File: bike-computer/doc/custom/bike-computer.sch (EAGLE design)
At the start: 12 parts, among them Q1 2N3820, Q2 2N3820, Q3 2N3820, X1 5566-8

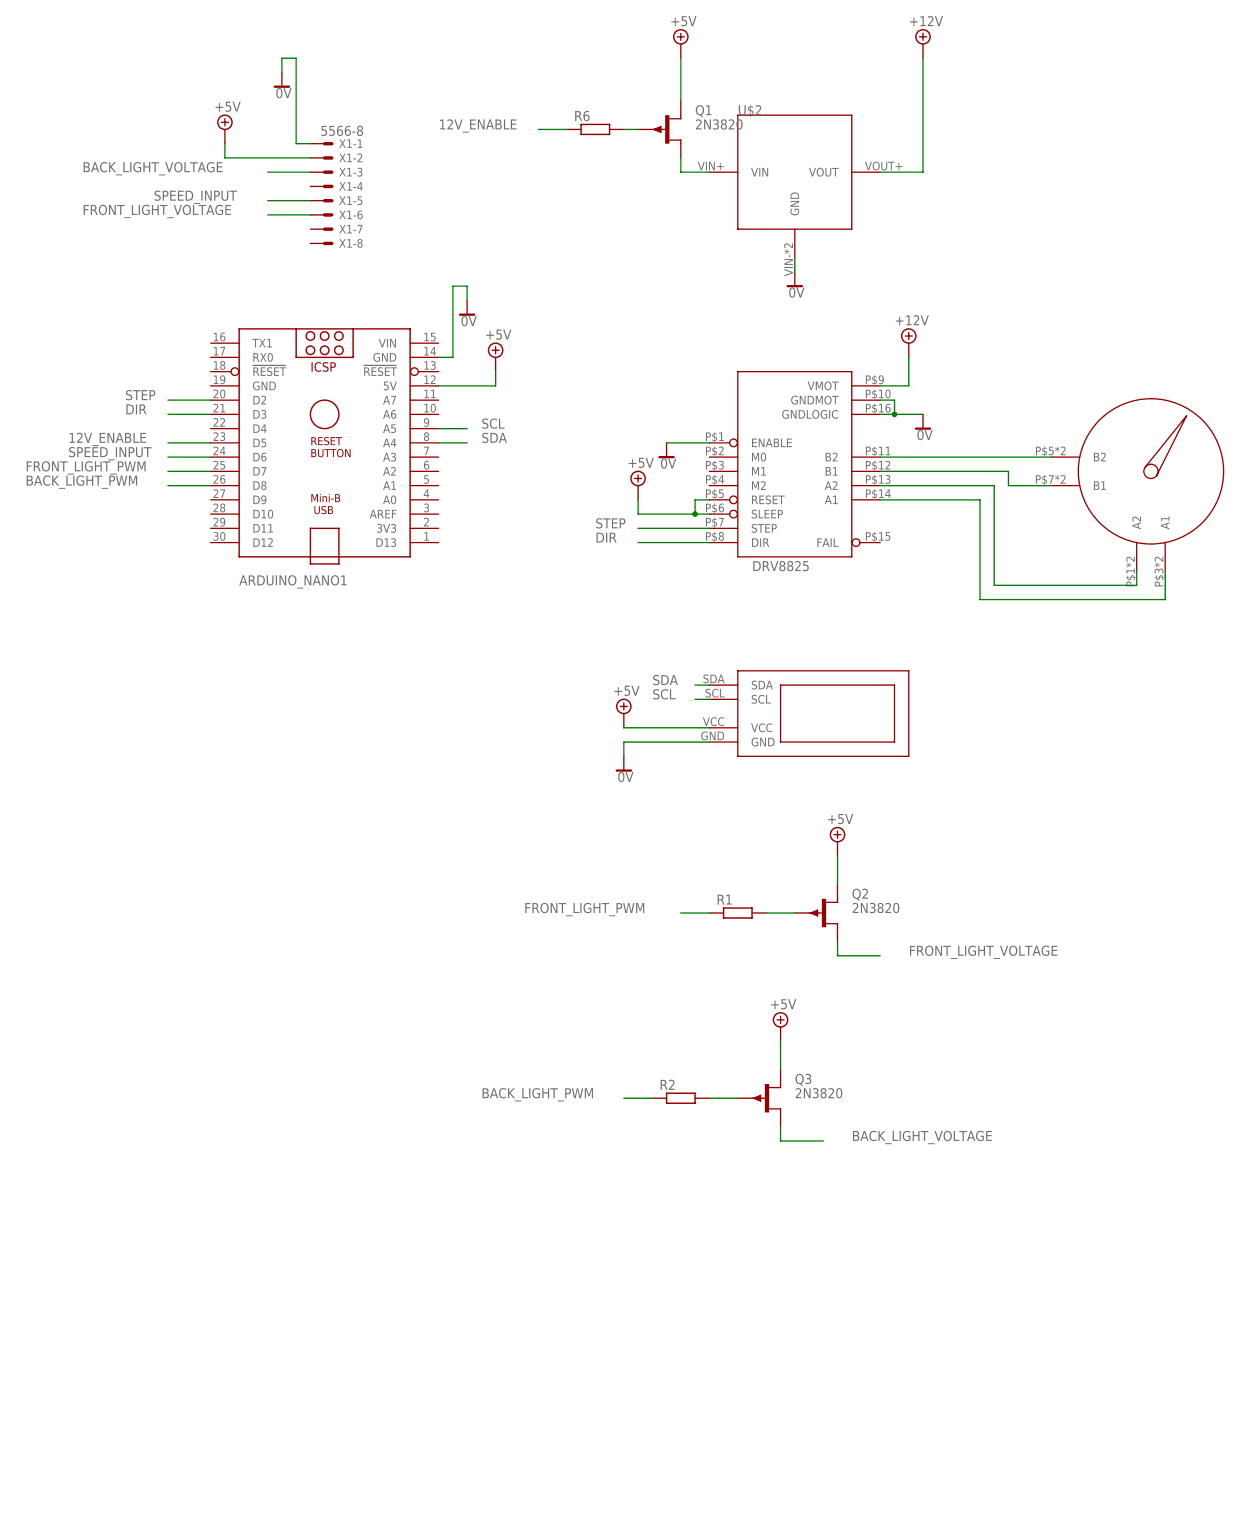
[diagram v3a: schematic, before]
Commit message: Change from Arduino Nano to Arduino Pro Mini.
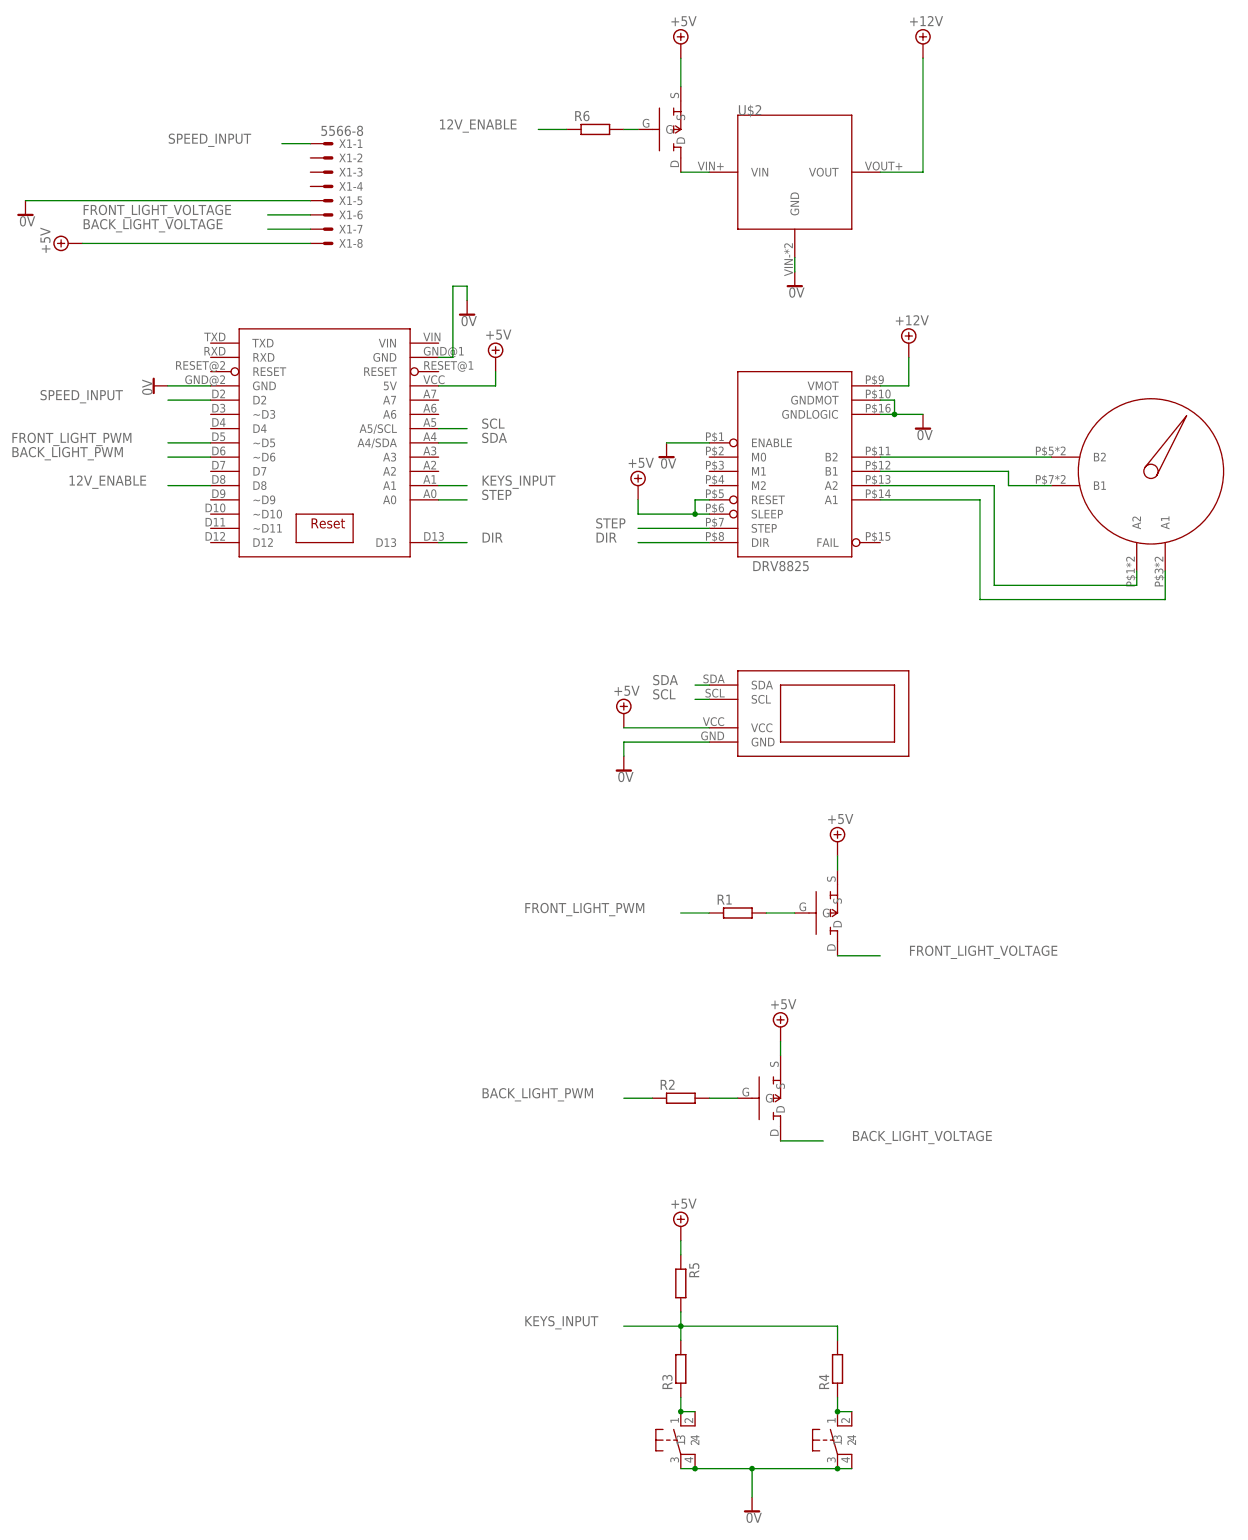
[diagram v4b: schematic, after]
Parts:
- removed ARDUINO_NANO1: (no value), ArduinoNanoV30:ARDUINO_NANO
- removed Q1, Q2, Q3: 2N3820, transistor-small-signal:2N3820
- added R3, R4, R5: (no value), rcl:R-EU_0204/5
- added U$4, U$5, U$6: BS250, bike_computer:BS250
- added U$7: (no value), bike_computer:ARDUINO_PRO_MINI
- added U$8, U$9: MICRO_SWITCH, bike_computer:MICRO_SWITCH
- R1: device rcl:R-EU_0204/5 -> rcl:R-EU_0617/17
- R2: device rcl:R-EU_0204/5 -> rcl:R-EU_0207/15
- R6: device rcl:R-EU_0204/5 -> rcl:R-EU_0207/10
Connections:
- new net KEYS_INPUT: R3.2, R4.2, R5.2, U$7.A1
- new net N$10: R3.1, U$8.1, U$8.2
- new net N$11: R4.1, U$9.1, U$9.2
- net +5V: now also R5.1, U$4.S, U$5.S, U$6.S, U$7.5V, X1-8.S; no longer ARDUINO_NANO1.5V, Q1.S, Q2.S, Q3.S, X1-2.S
- net 0V: now also U$7.GND@1, U$7.GND@2, U$8.3, U$8.4, U$9.3, U$9.4, X1-5.S; no longer ARDUINO_NANO1.GND@2, X1-1.S
- net 12V_ENABLE: now also U$7.D8; no longer ARDUINO_NANO1.D5
- net BACK_LIGHT_PWM: now also U$7.~D6; no longer ARDUINO_NANO1.D8
- net BACK_LIGHT_VOLTAGE: now also U$5.D, X1-7.S; no longer Q3.D, X1-3.S
- net DIR: now also U$7.D13; no longer ARDUINO_NANO1.D3
- net FRONT_LIGHT_PWM: now also U$7.~D5; no longer ARDUINO_NANO1.D7
- net FRONT_LIGHT_VOLTAGE: now also U$4.D; no longer Q2.D
- net N$5: now also U$4.G; no longer Q2.G
- net N$6: now also U$6.G; no longer Q1.G
- net N$7: now also U$6.D; no longer Q1.D
- net N$8: now also U$5.G; no longer Q3.G
- net SCL: now also U$7.A5/SCL; no longer ARDUINO_NANO1.A5
- net SDA: now also U$7.A4/SDA; no longer ARDUINO_NANO1.A4
- net SPEED_INPUT: now also U$7.D2, X1-1.S; no longer ARDUINO_NANO1.D6, X1-5.S
- net STEP: now also U$7.A0; no longer ARDUINO_NANO1.D2

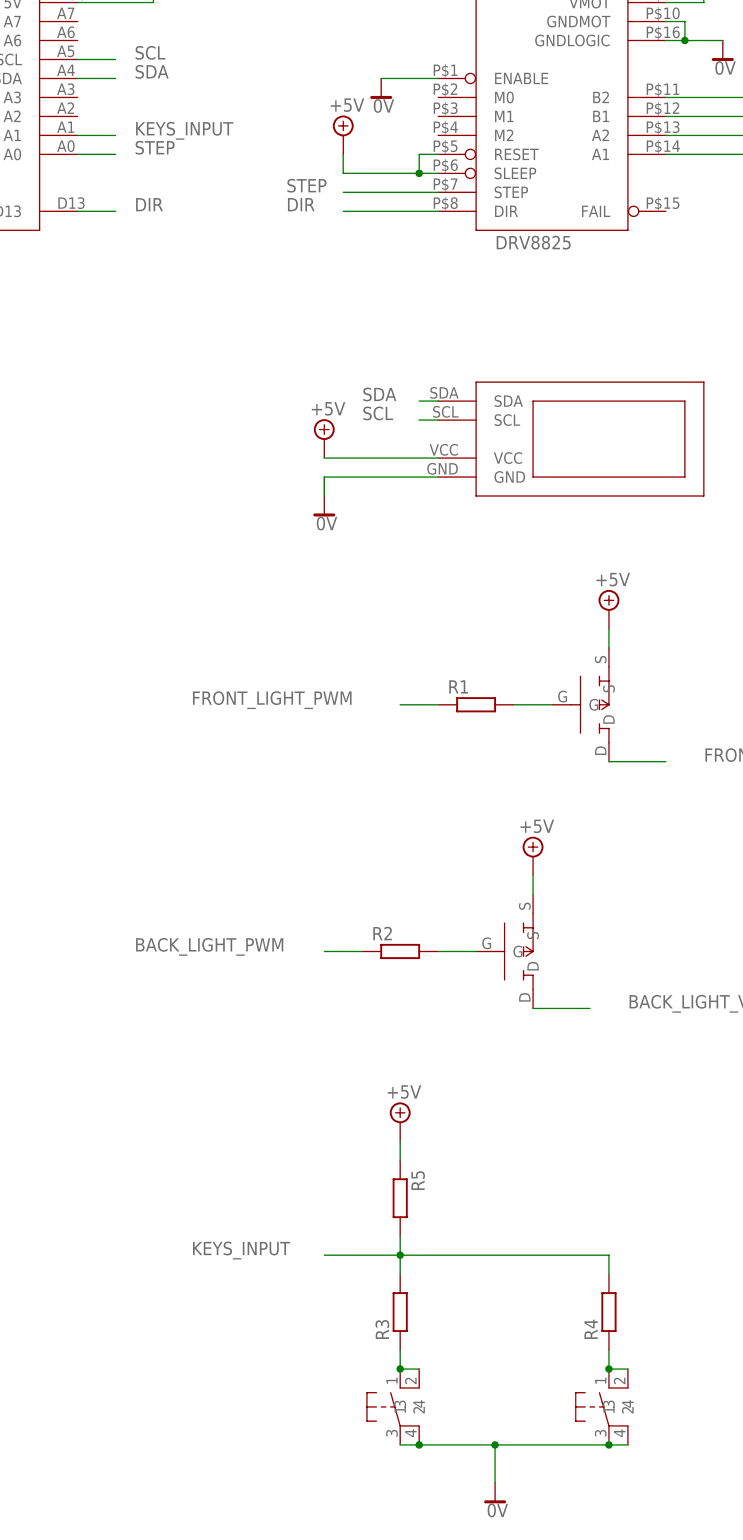
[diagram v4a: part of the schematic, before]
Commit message: [Bike] Further work on schematics.
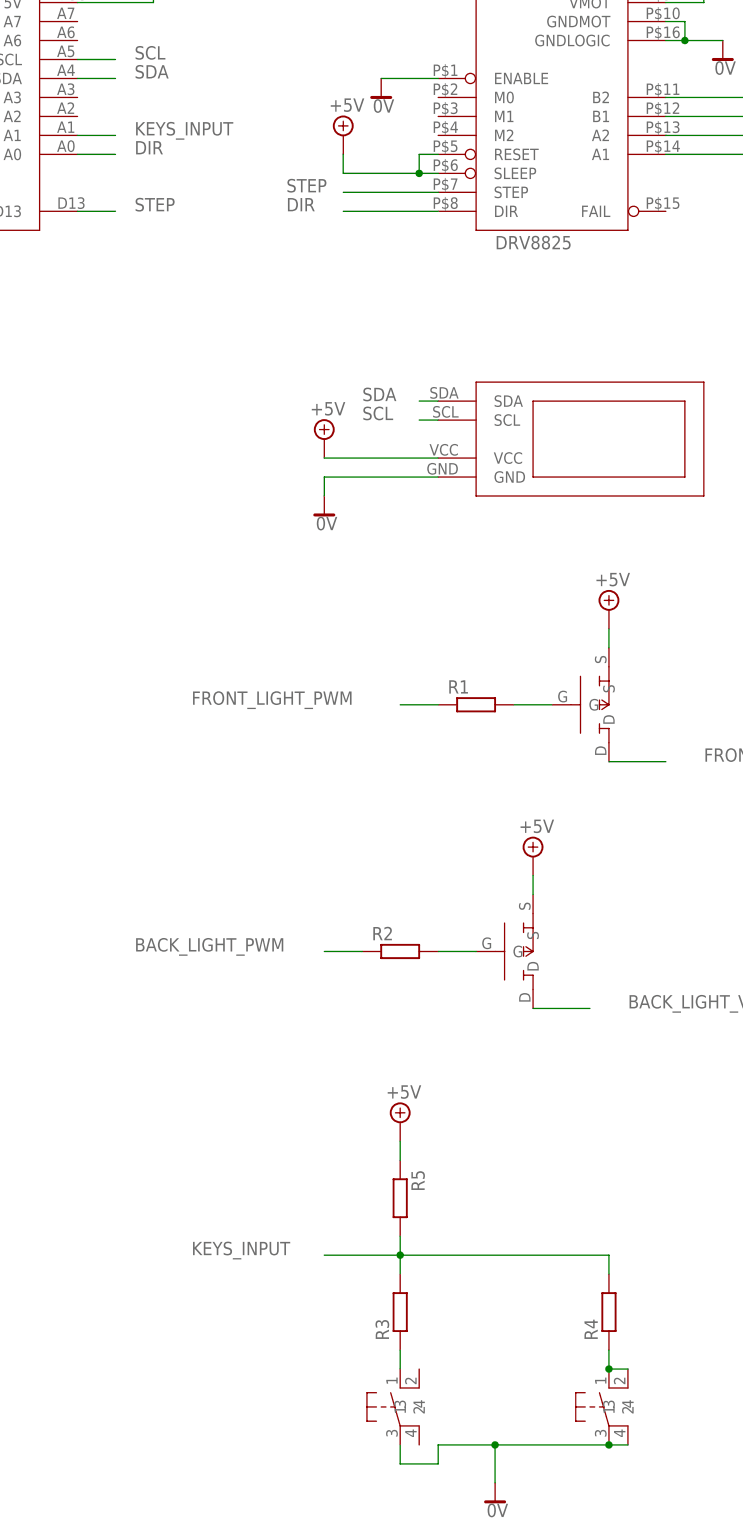
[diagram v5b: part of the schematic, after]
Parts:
- R3: device rcl:R-EU_0204/5 -> rcl:R-EU_0207/12
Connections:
- net 0V: no longer U$8.4
- net DIR: now also U$7.A0; no longer U$7.D13
- net N$10: no longer U$8.2
- net STEP: now also U$7.D13; no longer U$7.A0
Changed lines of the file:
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@@
 <part name="SUPPLY23" library="supply2" library_urn="urn:adsk.eagle:library:372" deviceset="+5V" device=""/>
 <part name="SUPPLY7" library="supply2" library_urn="urn:adsk.eagle:library:372" deviceset="0V" device=""/>
-<part name="R3" library="rcl" library_urn="urn:adsk.eagle:library:334" deviceset="R-EU_" device="0204/5" package3d_urn="urn:adsk.eagle:package:23488/1"/>
+<part name="R3" library="rcl" library_urn="urn:adsk.eagle:library:334" deviceset="R-EU_" device="0207/12" package3d_urn="urn:adsk.eagle:package:23489/1"/>
 <part name="R4" library="rcl" library_urn="urn:adsk.eagle:library:334" deviceset="R-EU_" device="0204/5" package3d_urn="urn:adsk.eagle:package:23488/1"/>
 <part name="R5" library="rcl" library_urn="urn:adsk.eagle:library:334" deviceset="R-EU_" device="0204/5" package3d_urn="urn:adsk.eagle:package:23488/1"/>
@@
 <pinref part="SUPPLY7" gate="0V" pin="0V"/>
 <wire x1="63.5" y1="-180.34" x2="63.5" y2="-175.26" width="0.1524" layer="91"/>
-<junction x="63.5" y="-175.26"/>
-<wire x1="53.34" y1="-175.26" x2="63.5" y2="-175.26" width="0.1524" layer="91"/>
-<pinref part="U$8" gate="G$1" pin="4"/>
 <wire x1="63.5" y1="-175.26" x2="78.74" y2="-175.26" width="0.1524" layer="91"/>
 <pinref part="U$9" gate="G$1" pin="3"/>
-<pinref part="U$8" gate="G$1" pin="3"/>
-<wire x1="53.34" y1="-175.26" x2="50.8" y2="-175.26" width="0.1524" layer="91"/>
-<junction x="53.34" y="-175.26"/>
 <pinref part="U$9" gate="G$1" pin="4"/>
 <wire x1="81.28" y1="-175.26" x2="78.74" y2="-175.26" width="0.1524" layer="91"/>
 <junction x="78.74" y="-175.26"/>
+<wire x1="63.5" y1="-175.26" x2="55.88" y2="-175.26" width="0.1524" layer="91"/>
+<junction x="63.5" y="-175.26"/>
+<wire x1="55.88" y1="-175.26" x2="55.88" y2="-177.8" width="0.1524" layer="91"/>
+<wire x1="55.88" y1="-177.8" x2="50.8" y2="-177.8" width="0.1524" layer="91"/>
+<pinref part="U$8" gate="G$1" pin="3"/>
+<wire x1="50.8" y1="-177.8" x2="50.8" y2="-175.26" width="0.1524" layer="91"/>
 </segment>
 <segment>
@@
 </segment>
 <segment>
-<wire x1="7.62" y1="-2.54" x2="12.7" y2="-2.54" width="0.1524" layer="91"/>
-<label x="15.24" y="-2.54" size="1.778" layer="95"/>
-<pinref part="U$7" gate="G$1" pin="A0"/>
+<pinref part="U$7" gate="G$1" pin="D13"/>
+<wire x1="7.62" y1="-10.16" x2="12.7" y2="-10.16" width="0.1524" layer="91"/>
+<label x="15.24" y="-10.16" size="1.778" layer="95"/>
 </segment>
 </net>
@@
 </segment>
 <segment>
-<wire x1="7.62" y1="-10.16" x2="12.7" y2="-10.16" width="0.1524" layer="91"/>
-<label x="15.24" y="-10.16" size="1.778" layer="95"/>
-<pinref part="U$7" gate="G$1" pin="D13"/>
+<pinref part="U$7" gate="G$1" pin="A0"/>
+<wire x1="7.62" y1="-2.54" x2="12.7" y2="-2.54" width="0.1524" layer="91"/>
+<label x="15.24" y="-2.54" size="1.778" layer="95"/>
 </segment>
 </net>
@@
 <wire x1="50.8" y1="-165.1" x2="50.8" y2="-162.56" width="0.1524" layer="91"/>
 <pinref part="U$8" gate="G$1" pin="1"/>
-<junction x="50.8" y="-165.1"/>
-<pinref part="U$8" gate="G$1" pin="2"/>
-<wire x1="50.8" y1="-165.1" x2="53.34" y2="-165.1" width="0.1524" layer="91"/>
 </segment>
 </net>
 <net name="N$11" class="0">
 <segment>
-<pinref part="R4" gate="G$1" pin="1"/>
-<wire x1="78.74" y1="-165.1" x2="78.74" y2="-162.56" width="0.1524" layer="91"/>
 <pinref part="U$9" gate="G$1" pin="1"/>
-<junction x="78.74" y="-165.1"/>
 <pinref part="U$9" gate="G$1" pin="2"/>
 <wire x1="81.28" y1="-165.1" x2="78.74" y2="-165.1" width="0.1524" layer="91"/>
+<pinref part="R4" gate="G$1" pin="1"/>
+<wire x1="78.74" y1="-162.56" x2="78.74" y2="-165.1" width="0.1524" layer="91"/>
+<junction x="78.74" y="-165.1"/>
 </segment>
 </net>
 <net name="KEYS_INPUT" class="0">
 <segment>
-<pinref part="R4" gate="G$1" pin="2"/>
-<wire x1="78.74" y1="-152.4" x2="78.74" y2="-149.86" width="0.1524" layer="91"/>
 <wire x1="78.74" y1="-149.86" x2="50.8" y2="-149.86" width="0.1524" layer="91"/>
 <pinref part="R3" gate="G$1" pin="2"/>
@@
 <wire x1="50.8" y1="-149.86" x2="40.64" y2="-149.86" width="0.1524" layer="91"/>
 <label x="22.86" y="-149.86" size="1.778" layer="95"/>
-</segment>
-<segment>
+<pinref part="R4" gate="G$1" pin="2"/>
+<wire x1="78.74" y1="-149.86" x2="78.74" y2="-152.4" width="0.1524" layer="91"/>
+</segment>
+<segment>

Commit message: [Bike] More work on schematics.
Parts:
- R6: device rcl:R-EU_0207/10 -> rcl:R-EU_0207/15
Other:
- moved on the sheet: DRV8825
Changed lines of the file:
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@@
 <part name="R1" library="rcl" library_urn="urn:adsk.eagle:library:334" deviceset="R-EU_" device="0617/17" package3d_urn="urn:adsk.eagle:package:23575/2"/>
 <part name="R2" library="rcl" library_urn="urn:adsk.eagle:library:334" deviceset="R-EU_" device="0207/15" package3d_urn="urn:adsk.eagle:package:23492/1"/>
-<part name="R6" library="rcl" library_urn="urn:adsk.eagle:library:334" deviceset="R-EU_" device="0207/10" package3d_urn="urn:adsk.eagle:package:23491/2"/>
+<part name="R6" library="rcl" library_urn="urn:adsk.eagle:library:334" deviceset="R-EU_" device="0207/15" package3d_urn="urn:adsk.eagle:package:23492/1"/>
 <part name="SUPPLY23" library="supply2" library_urn="urn:adsk.eagle:library:372" deviceset="+5V" device=""/>
 <part name="SUPPLY7" library="supply2" library_urn="urn:adsk.eagle:library:372" deviceset="0V" device=""/>
